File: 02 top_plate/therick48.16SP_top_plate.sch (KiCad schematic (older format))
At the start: 85 parts, among them U1 HOLE, U10 HOLE, U11 HOLE, U12 HOLE, U13 HOLE, U14 HOLE, U15 HOLE, U16 HOLE, U17 HOLE, U18 HOLE, U19 HOLE, U2 HOLE, U20 HOLE, U21 HOLE, U22 HOLE, U23 HOLE, U24 HOLE, U25 HOLE, U26 HOLE, U27 HOLE, U28 HOLE, U29 HOLE, U3 HOLE, U30 HOLE, U31 HOLE, U32 HOLE, U33 HOLE, U34 HOLE, U35 HOLE, U36 HOLE, U37 HOLE, U38 HOLE, U39 HOLE, U4 HOLE, U40 HOLE, U41 HOLE, U42 HOLE, U43 HOLE, U44 HOLE, U45 HOLE, U46 HOLE, U47 HOLE, U48 HOLE, U49 HOLE, U5 HOLE, U50 HOLE, U51 HOLE, U52 HOLE, U53 HOLE, U54 HOLE, U55 HOLE, U56 HOLE, U57 HOLE, U58 HOLE, U59 HOLE, U6 HOLE, U60 HOLE, U61 HOLE, U62 HOLE, U63 HOLE, U64 HOLE, U65 HOLE, U66 HOLE, U67 HOLE, U7 HOLE, U8 HOLE, U9 HOLE

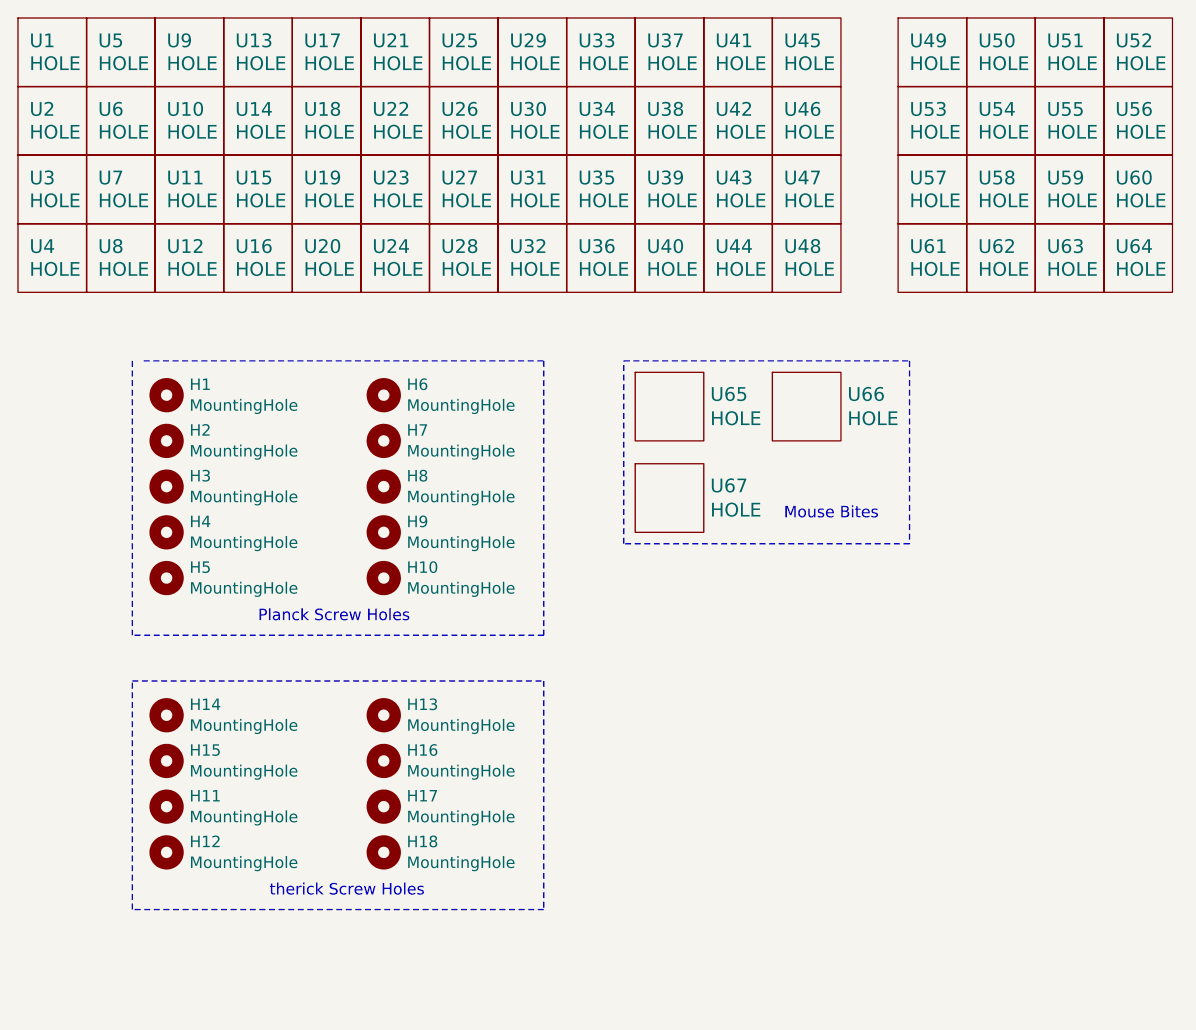
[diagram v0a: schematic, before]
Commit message: Added breakaway section, added rotary encoder support
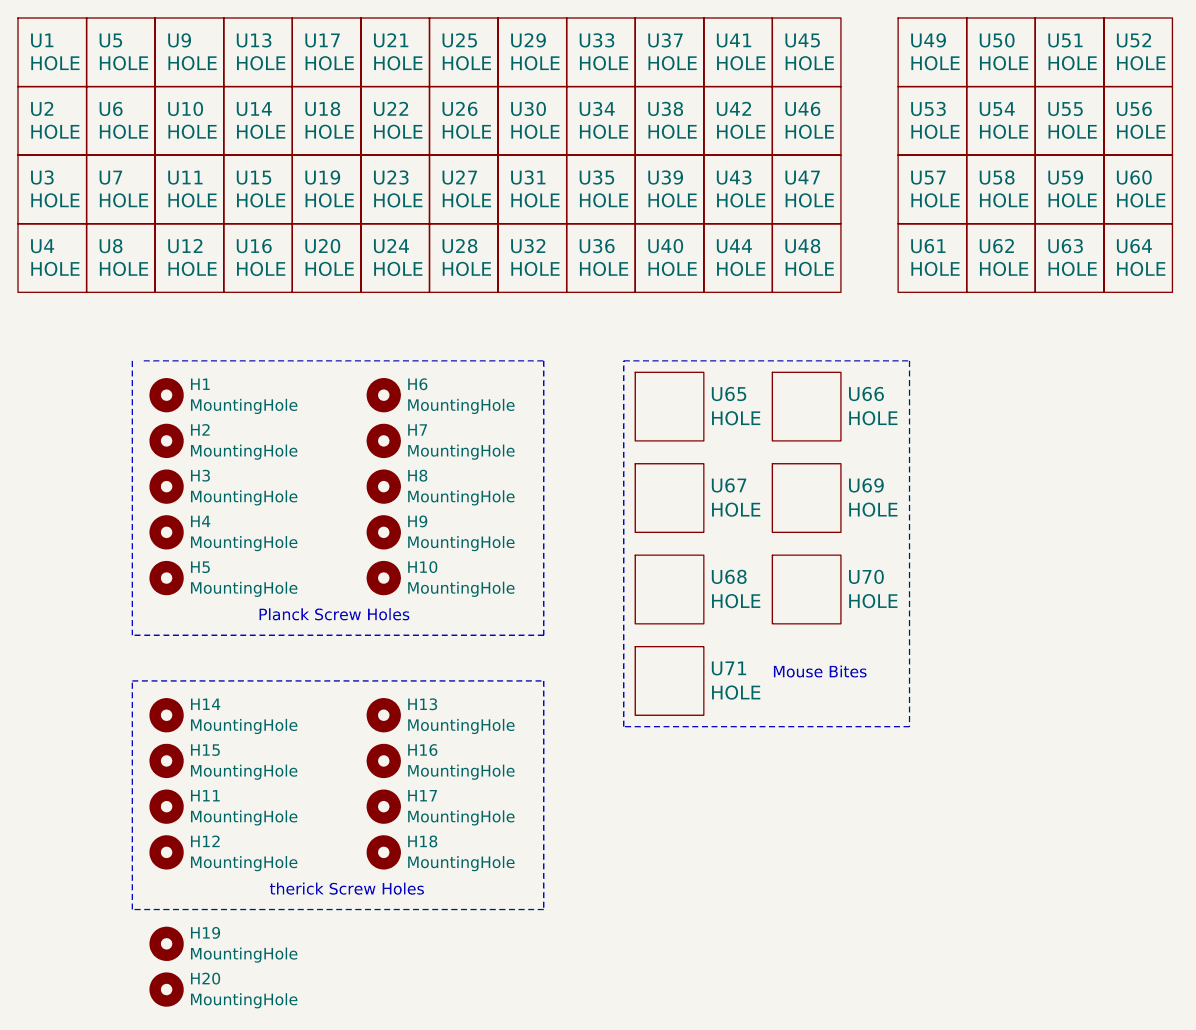
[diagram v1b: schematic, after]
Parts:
- added H19, H20: MountingHole, random-keyboard-parts:plate_hole_4mm_tht, symbol Mechanical:MountingHole
- added U68, U69, U70, U71: HOLE, acheron_Hardware:MouseBite_IPC7351, symbol lets_split-cache:HOLE
